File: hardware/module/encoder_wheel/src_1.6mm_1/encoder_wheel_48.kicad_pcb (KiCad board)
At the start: 2 copper layers, 74 x 74 mm, 2 parts

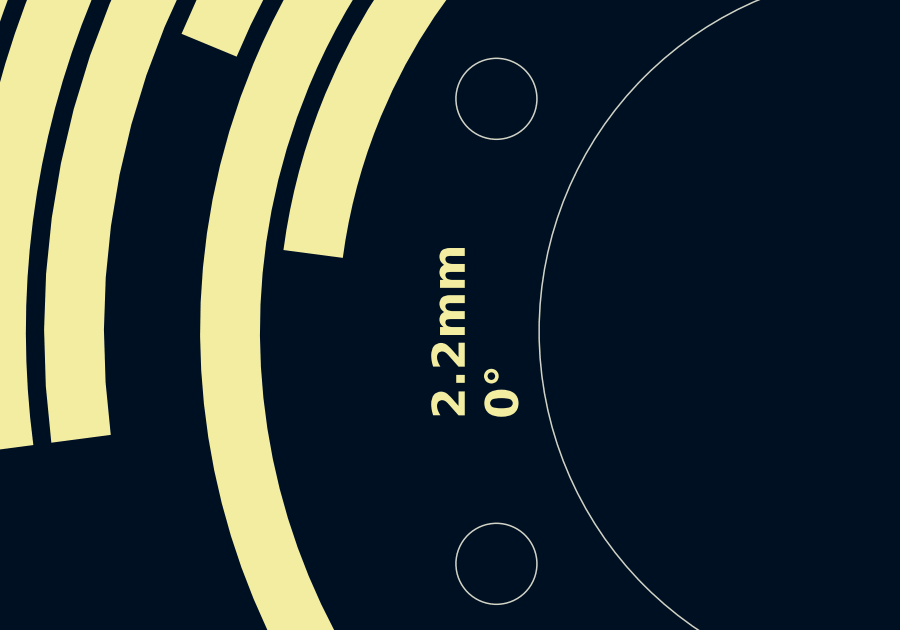
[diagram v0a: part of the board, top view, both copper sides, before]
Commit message: add encoder wheel variants
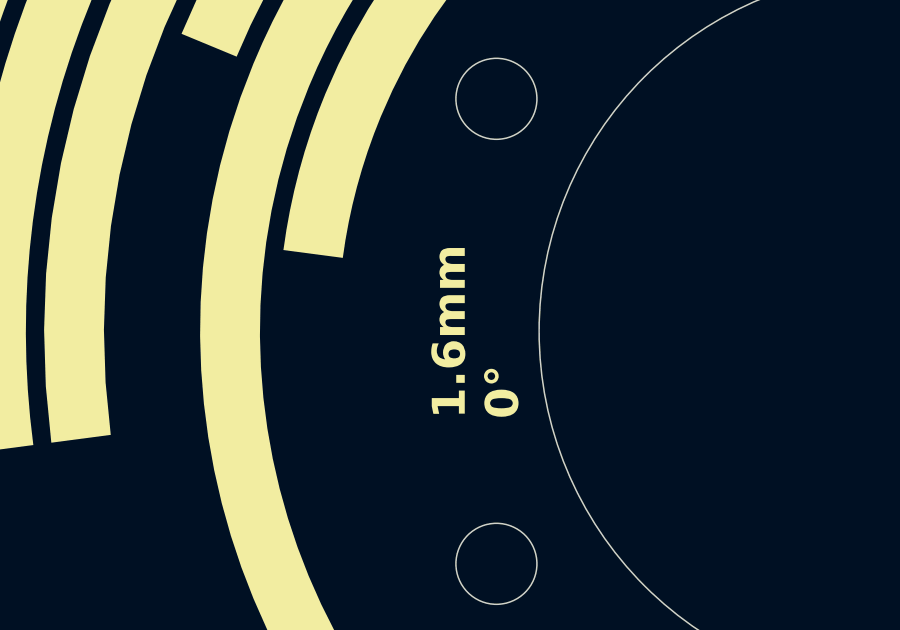
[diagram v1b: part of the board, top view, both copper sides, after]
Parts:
- REF** (x2): value OpenFlapEncoderPattern48_2.2mm -> OpenFlapEncoderPattern48_1.6mm; footprint EncoderPattern:OpenFlapEncoderPattern48_2.2mm -> EncoderPattern:OpenFlapEncoderPattern48_1.6mm
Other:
- board text added: "1.6mm 0°"
- board text added: "1.6mm 3.75°"
- board text removed: "2.2mm 0°"
- board text removed: "2.2mm 3.75°"
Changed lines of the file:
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@@
 	)
 	(net 0 "")
-	(footprint "EncoderPattern:OpenFlapEncoderPattern48_2.2mm"
+	(footprint "EncoderPattern:OpenFlapEncoderPattern48_1.6mm"
 		(layer "F.Cu")
 		(at 101 100)
@@
 			)
 		)
-		(property "Value" "OpenFlapEncoderPattern48_2.2mm"
+		(property "Value" "OpenFlapEncoderPattern48_1.6mm"
 			(at 0 1 0)
 			(unlocked yes)
@@
 			)
 		)
-		(property "Footprint" "EncoderPattern:OpenFlapEncoderPattern48_2.2mm"
+		(property "Footprint" "EncoderPattern:OpenFlapEncoderPattern48_1.6mm"
 			(at 0 0 0)
 			(unlocked yes)
@@
 		)
 	)
-	(footprint "EncoderPattern:OpenFlapEncoderPattern48_2.2mm"
+	(footprint "EncoderPattern:OpenFlapEncoderPattern48_1.6mm"
 		(layer "B.Cu")
 		(at 101 100 -176.25)
@@
 			)
 		)
-		(property "Value" "OpenFlapEncoderPattern48_2.2mm"
+		(property "Value" "OpenFlapEncoderPattern48_1.6mm"
 			(at 0 -1 3.75)
 			(unlocked yes)
@@
 			)
 		)
-		(property "Footprint" "EncoderPattern:OpenFlapEncoderPattern48_2.2mm"
+		(property "Footprint" "EncoderPattern:OpenFlapEncoderPattern48_1.6mm"
 			(at 0 0 3.75)
 			(unlocked yes)
@@
 		(layer "Edge.Cuts")
 	)
-	(gr_text "2.2mm \n3.75°"
+	(gr_text "1.6mm \n3.75°"
 		(at 88.427 97.333 90)
 		(layer "B.SilkS")
@@
 		)
 	)
-	(gr_text "2.2mm \n0°"
+	(gr_text "1.6mm \n0°"
 		(at 88.427 102.921 90)
 		(layer "F.SilkS")

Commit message: encoder changes
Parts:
- renumbered REF** to ENC1, REF** to ENC2

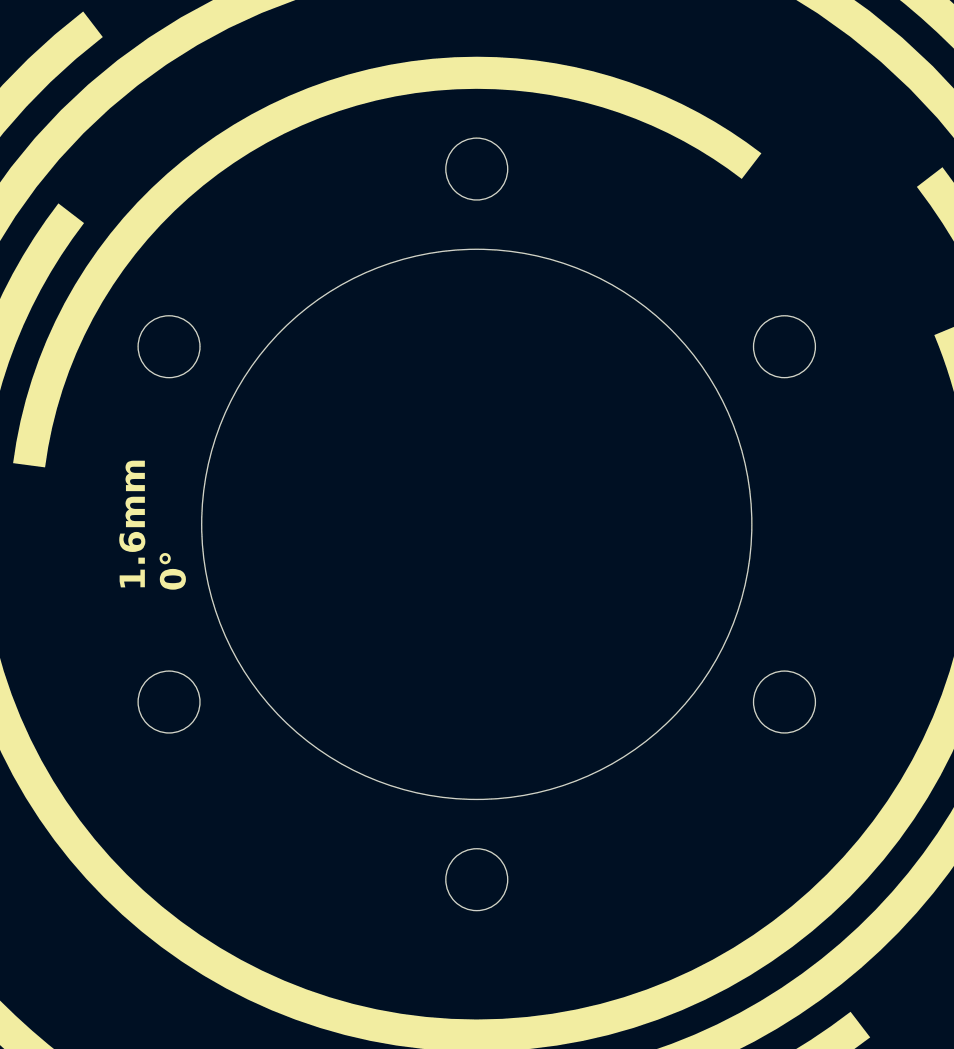
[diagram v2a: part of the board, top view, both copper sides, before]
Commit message: changed hole patern encoder wheel
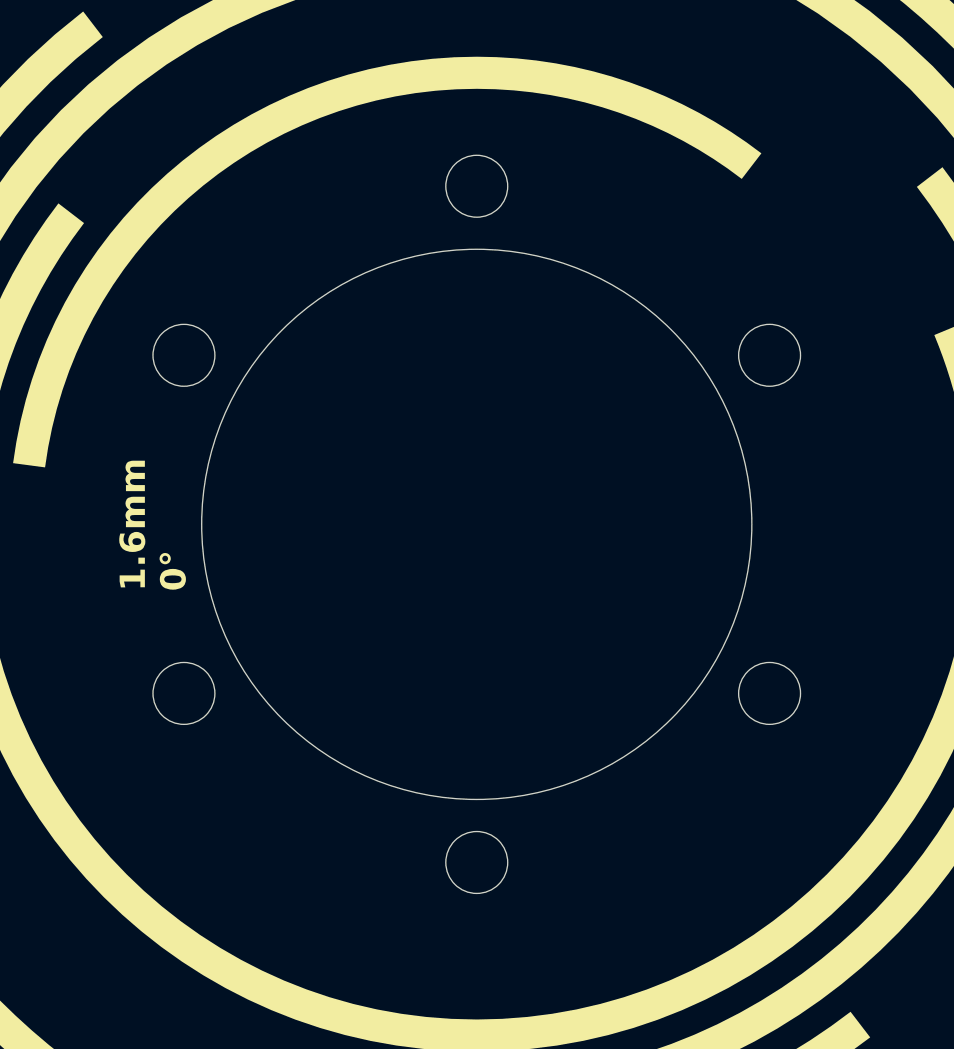
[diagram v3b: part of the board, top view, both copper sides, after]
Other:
- outline, holes or cut-outs redrawn
